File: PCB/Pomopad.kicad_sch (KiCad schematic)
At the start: 22 parts, among them J1 OLED, SW1 RotaryEncoder_Switch, SW2 SW_Push, SW3 SW_Push, SW4 SW_Push, SW5 SW_Push, SW6 SW_Push, SW7 SW_Push, U1 MOUDLE-SEEEDUINO-XIAO

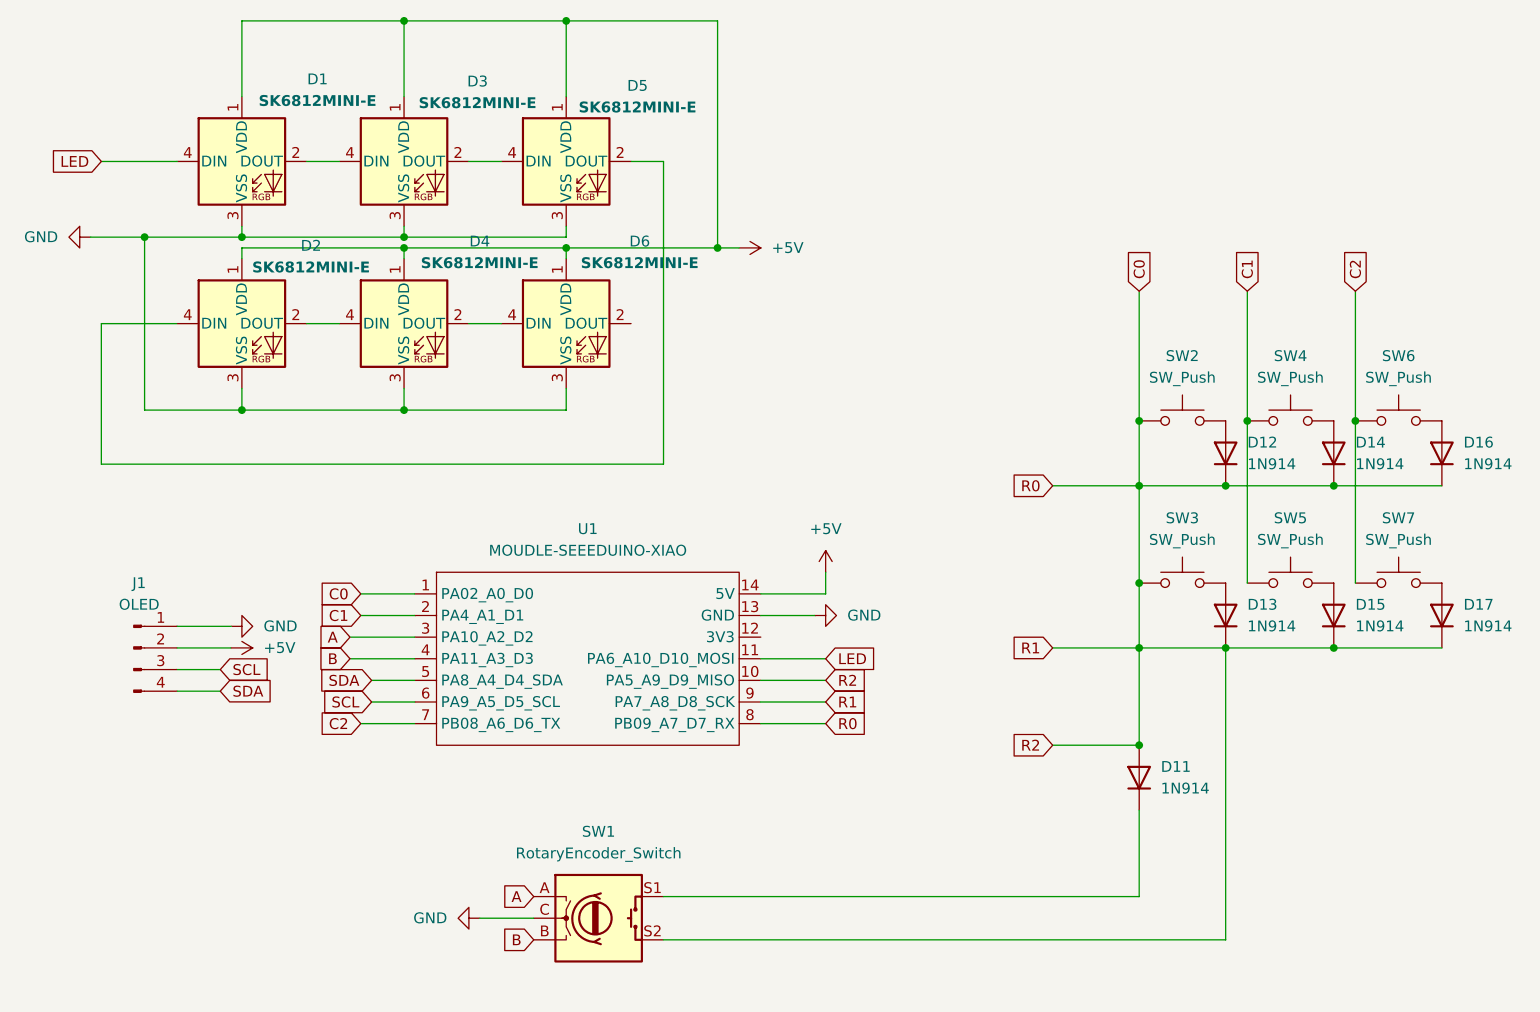
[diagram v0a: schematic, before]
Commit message: Updated firmware: moved encoder push into matrix, set diode direction COL2ROW
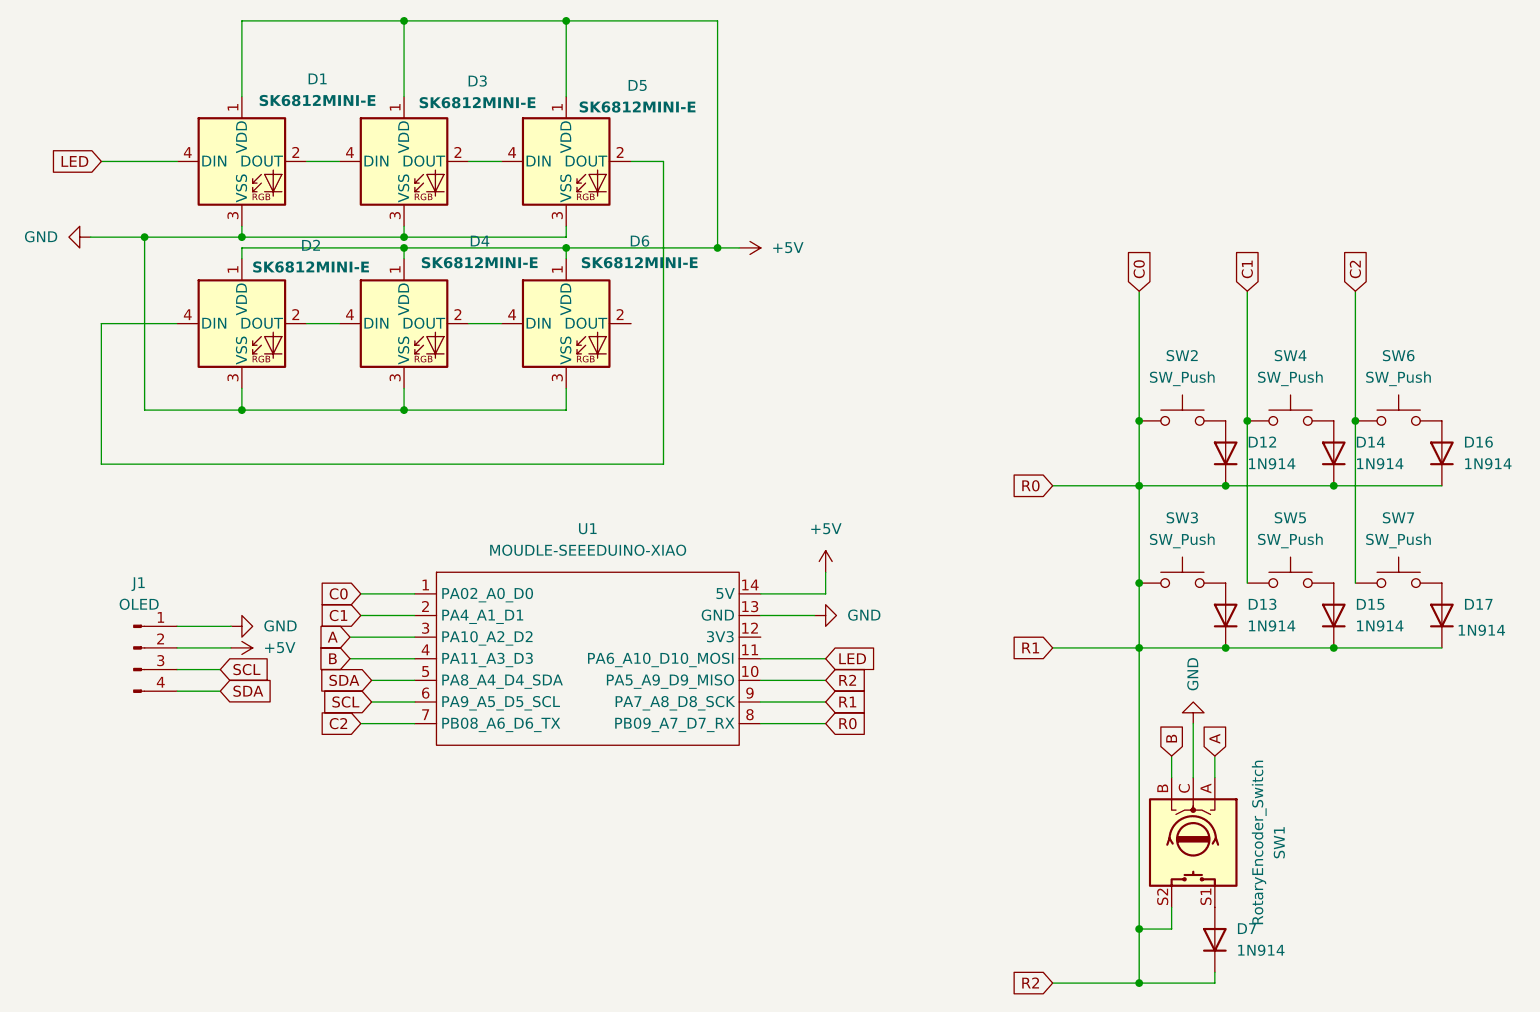
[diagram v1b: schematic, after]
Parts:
- removed D11: 1N914, Diode_THT:D_DO-35_SOD27_P7.62mm_Horizontal, symbol Diode:1N914
- added D7: 1N914, Diode_THT:D_DO-35_SOD27_P7.62mm_Horizontal, symbol Diode:1N914
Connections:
- net C0: now also D7.1 (K)
- net at SW1.S1: now also D7.2 (A)
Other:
- moved on the sheet: SW1
